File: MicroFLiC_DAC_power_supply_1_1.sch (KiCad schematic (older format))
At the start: 61 parts, among them P1 Socket_1x2, P2 Header_1x2, P3 Socket_2x4, U1 AP1117D50, U2 AP1117, U3 AP1117, U4 LM317, U5 LM317

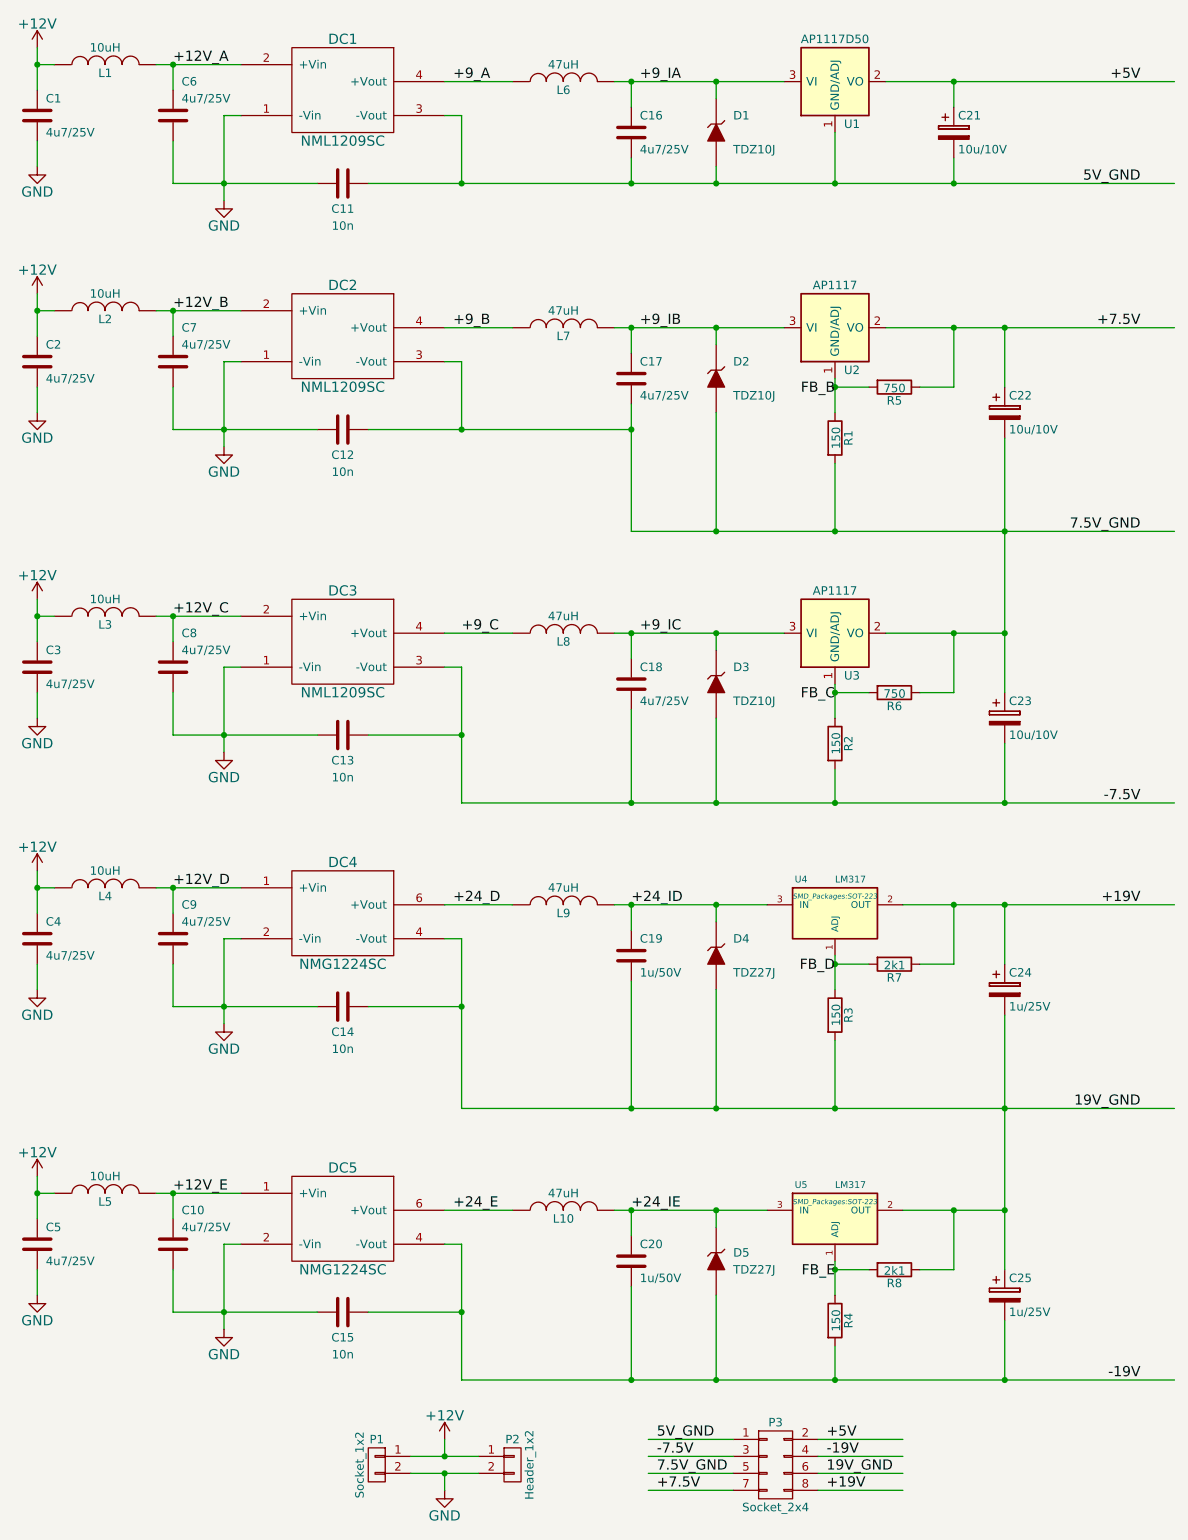
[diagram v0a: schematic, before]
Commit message: Completed part descriptions
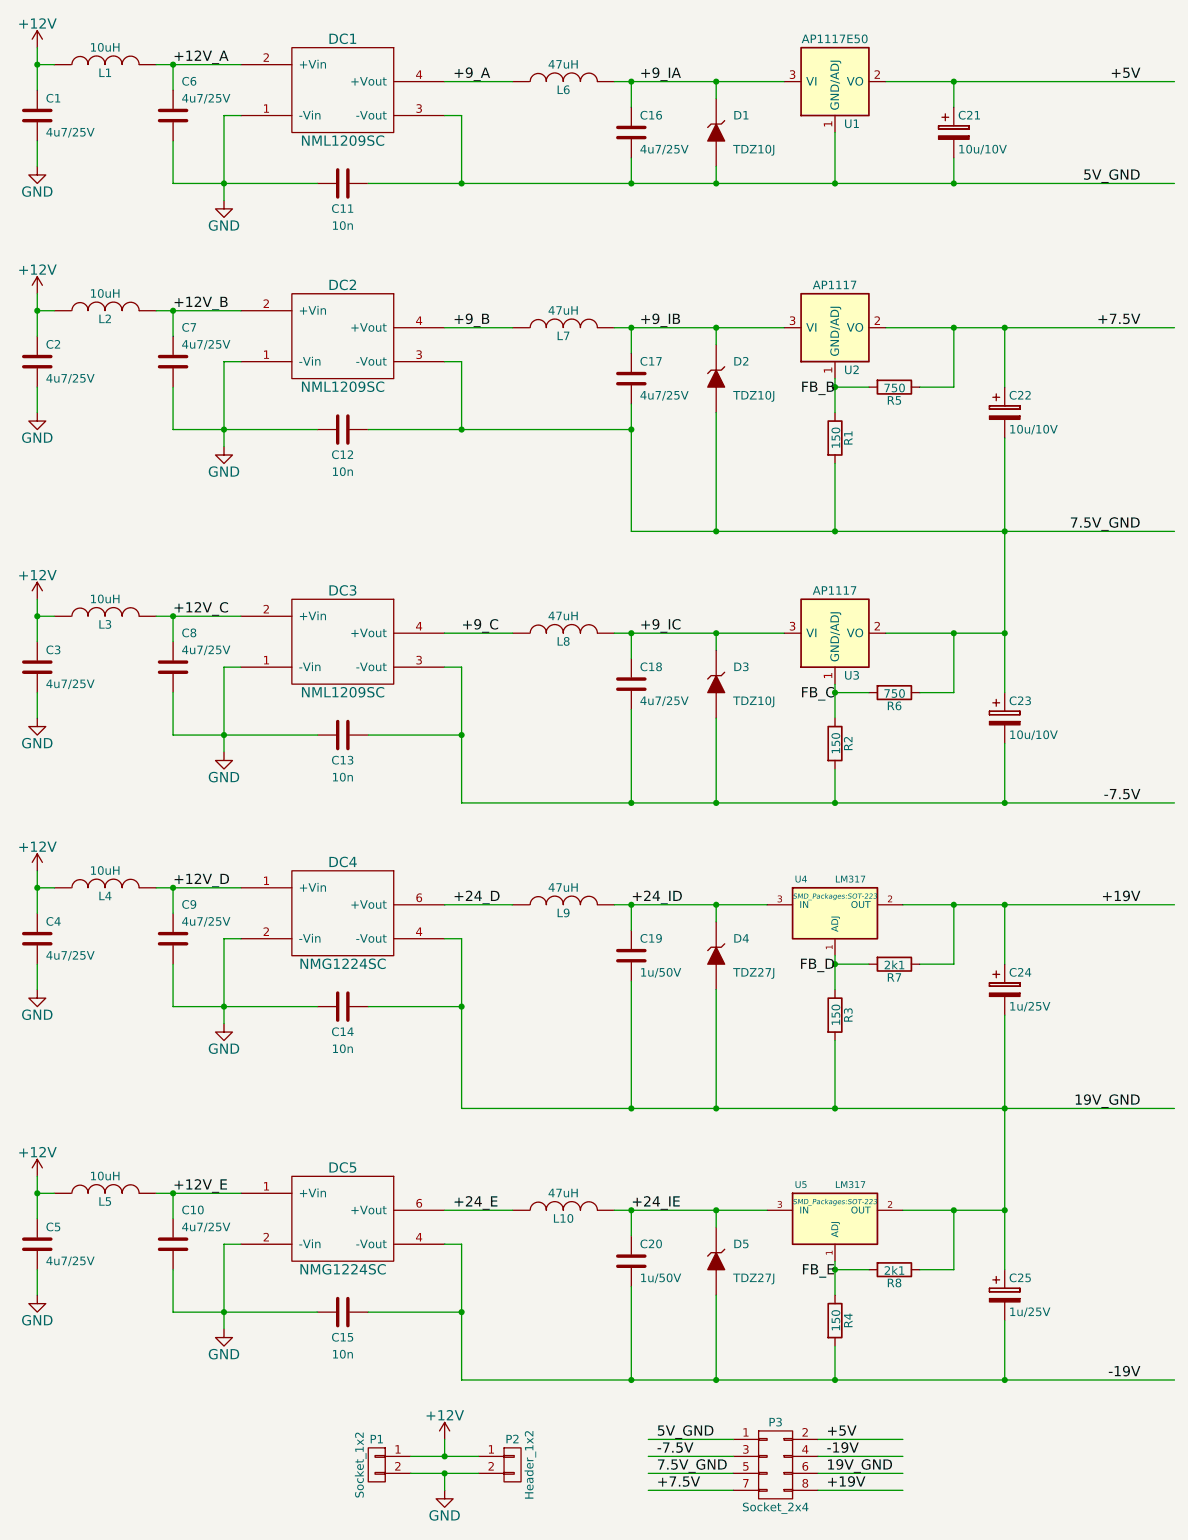
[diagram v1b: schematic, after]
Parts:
- C1, C10, C16, C17, C18, C2, C3, C4, C5, C6, C7, C8, C9: Alt. Order Code (none) -> 81-GRM21BR61E475MA2L; Alt. Supplier (none) -> Mouser; Note (none) -> 4μ7/25V X5R 0805 ceramic capacitor; Package (none) -> 0805; Supplier (none) -> Farnell
- C11, C12, C13, C14, C15: Note (none) -> Optional 10 nF X7R ceramic capacitor; Package (none) -> 0805; Supplier (none) -> Farnell
- C19, C20: Alt. Order Code (none) -> 81-GRM219R61H105KA3D; Alt. Supplier (none) -> Mouser; Note (none) -> 1μ/50V X5R 0805 ceramic capacitor; Package (none) -> 0805; Supplier (none) -> Farnell
- C21, C22, C23: Alt. Order Code (none) -> 581-TAJA106K010; Alt. Supplier (none) -> Mouser; Note (none) -> 10μF/10V/3Ω ESR tantalum capacitor; Package (none) -> case A; Supplier (none) -> Farnell
- C24, C25: Note (none) -> 1μ/25V/6.6Ω ESR tantalum capacitor; Package (none) -> case A; Supplier (none) -> Farnell
- D1, D2, D3: Alt. Order Code (none) -> 771-TDZ10J115; Alt. Supplier (none) -> Mouser; Note (none) -> 10V Zener diode; Package (none) -> SOD-323; Supplier (none) -> Farnell
- D4: Alt. Order Code (none) -> 771-TDZ27J115; Alt. Supplier (none) -> Mouser; Note (none) -> 27V Zener diode; Package (none) -> SOD-323; Supplier (none) -> Farnell
- D5: Alt. Order Code (none) -> 771-TDZ27J115; Alt. Supplier (none) -> Mouser; Note (none) -> 27V Zener diode; Package (none) -> SOD-323; Part Number (none) -> TDZ27J; Pert Number TDZ27J -> (none); Supplier (none) -> Farnell
- DC1, DC2, DC3: Alt. Order Code (none) -> 580-NML1209SC; Alt. Supplier (none) -> Mouser; Note (none) -> 12V in 9V out 2W DC-DC converter; Package (none) -> SIP-4; Supplier (none) -> Farnell
- DC4, DC5: Alt. Order Code (none) -> 81-NMG1224SC; Alt. Supplier (none) -> Mouser; Note (none) -> 12V in 24V out 2W DC-DC converter; Package (none) -> SIP-7; Supplier (none) -> Farnell
- L1, L2, L3, L4, L5: Alt. Order Code (none) -> 710-7440329100; Alt. Supplier (none) -> Mouser; Note (none) -> 10μH/0.45A SMD coil; Package (none) -> 1210; Supplier (none) -> Farnell
- L10, L6, L7, L8, L9: Alt. Order Code (none) -> 580-82473C; Alt. Supplier (none) -> Mouser; Note (none) -> 47μH/0.25A SMD coil; Package (none) -> 1210; Supplier (none) -> Farnell
- P1: Note (none) -> 1x2 ESQ series elevated socket strip; Package (none) -> SIL-2; Supplier (none) -> Farnell
- P2: Alt. Order Code (none) -> 855-M20-9990245; Alt. Supplier (none) -> Mouser; Note (none) -> 1x2 header strip; Package (none) -> SIL-2; Supplier (none) -> Farnell
- P3: Note (none) -> 2x4 ESQ series elevated socket strip; Package (none) -> DIL-8; Supplier (none) -> Farnell
- R1, R2, R3, R4: Note (none) -> 150Ω/1% 0805 resistor; Package (none) -> 0805; Supplier (none) -> Farnell
- R5: Note (none) -> 750Ω/1% 0805 resistor; Package (none) -> 0805; Supplier (none) -> Farnell
- R6: Note (none) -> 750Ω/1% 0805 resistor; Supplier (none) -> Farnell
- R7, R8: Alt. Order Code (none) -> 71-CRCW0805-2.1K-E3; Alt. Supplier (none) -> Mouser; Note (none) -> 2.1kΩ/1% 0805 resistor; Package (none) -> 0805; Supplier (none) -> Farnell
- U1: value AP1117D50 -> AP1117E50; Alt. Order Code (none) -> 621-AP1117E50G-13; Alt. Supplier (none) -> Mouser; Note (none) -> 5V linear voltage regulator; Package (none) -> SOT-223; Supplier (none) -> Farnell
- U2, U3: Alt. Order Code (none) -> 621-AP1117EG-13; Alt. Supplier (none) -> Mouser; Note (none) -> Adjustable linear voltage regulator; Package (none) -> SOT-223; Supplier (none) -> Farnell
- U4, U5: Alt. Order Code (none) -> 595-LM317DCY; Alt. Supplier (none) -> Mouser; Note (none) -> Adjustable linear voltage regulator; Package (none) -> SOT-223; Supplier (none) -> Farnell

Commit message: Added feedback filtering capacitors and protection diodes
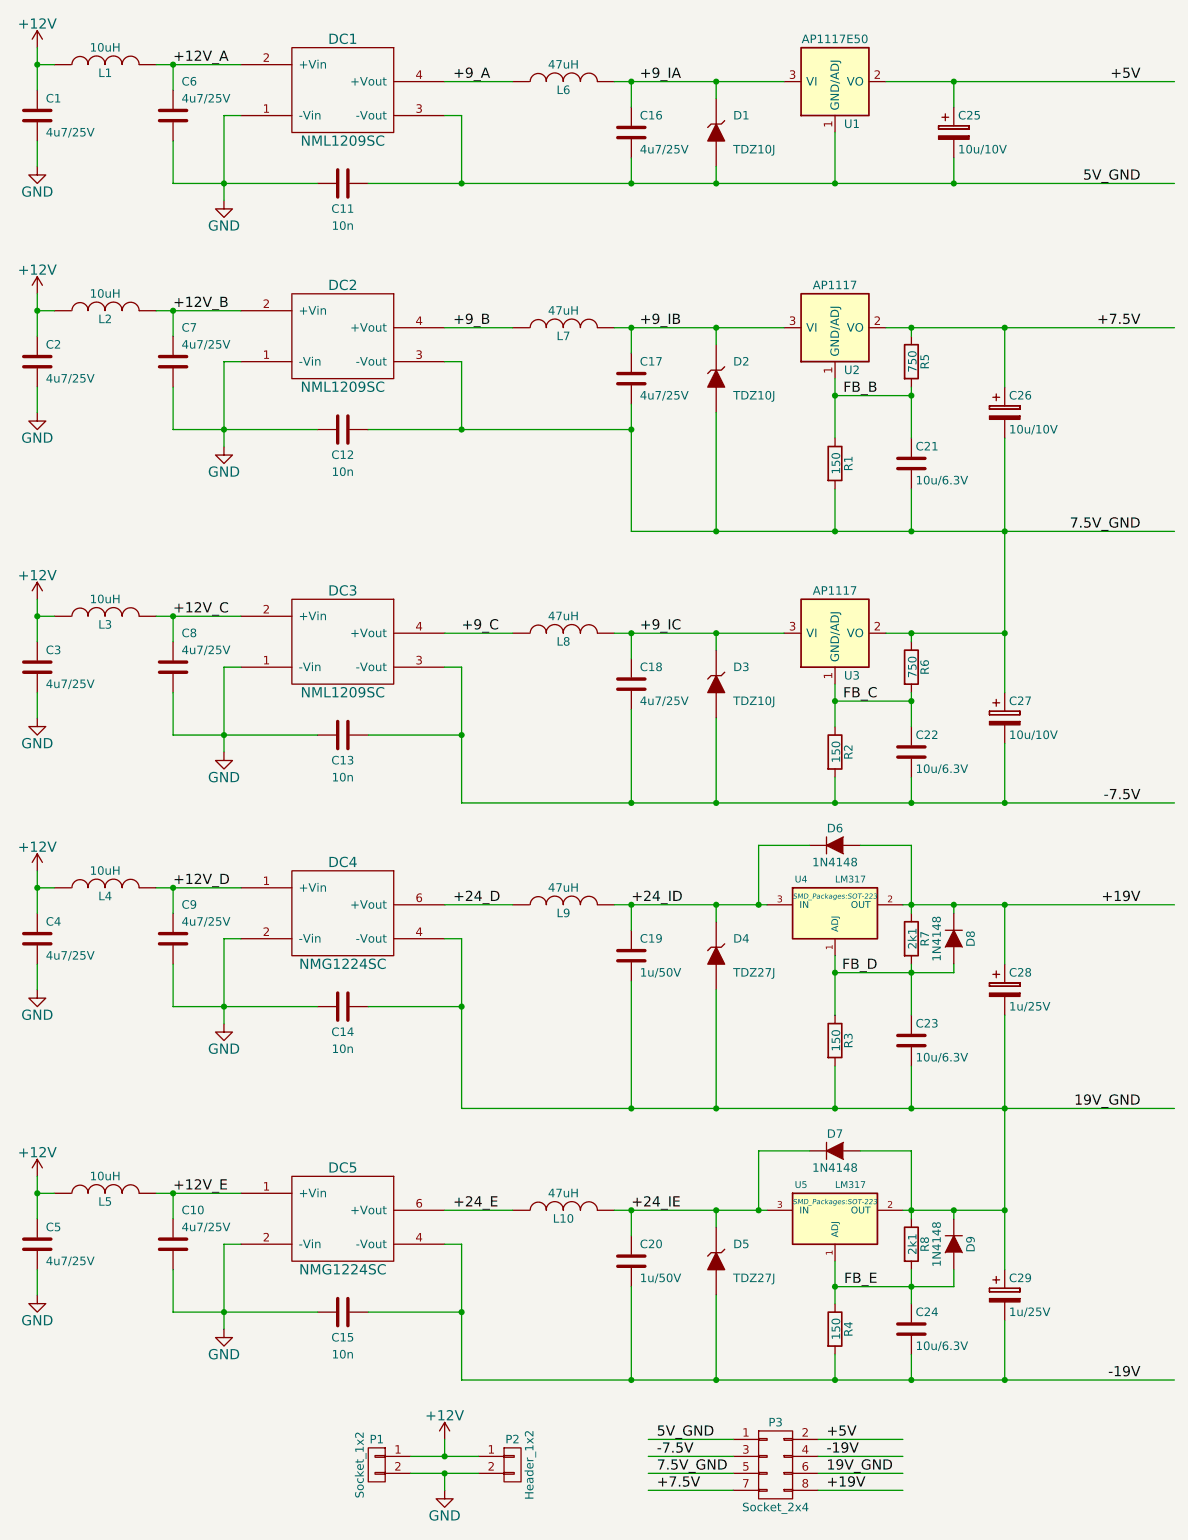
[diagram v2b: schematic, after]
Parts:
- added C21, C22, C23, C24: 10u/6.3V, Capacitors_SMD:C_0805, symbol C
- added D6, D7, D8, D9: 1N4148, Diodes_SMD:SOD-323, symbol D
- C11, C12, C13, C14, C15: Alt. Order Code (none) -> 80-C0805C103K5R; Alt. Supplier (none) -> Mouser
- C28: renamed from C24; Alt. Order Code (none) -> 74-TMCMA1E105MTRF; Alt. Supplier (none) -> Mouser
- C29: renamed from C25; Alt. Order Code (none) -> 74-TMCMA1E105MTRF; Alt. Supplier (none) -> Mouser
- P1: Alt. Order Code (none) -> ESQ-102-33-G-S; Alt. Supplier (none) -> Samtec
- P3: Alt. Order Code (none) -> ESQ-104-33-G-D; Alt. Supplier (none) -> Samtec
- R1, R2, R3, R4: Alt. Order Code (none) -> 71-TNPW0805150RFEEA; Alt. Supplier (none) -> Mouser
- R5, R6: Alt. Order Code (none) -> 603-RT0805FRE07750RL; Alt. Supplier (none) -> Mouser
- renumbered C21 to C25, C22 to C26, C23 to C27
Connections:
- wire segments 140 -> 154
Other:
- moved on the sheet: R1, R2, R3, R4, R5, R6, R7, R8

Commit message: Fixed capacitor order code
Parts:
- C11, C12, C13, C14, C15: Order Code 9306352 -> 9406352
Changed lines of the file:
@@
 F 6 "0805" H 2500 1600 60  0001 C CNN "Package"
 F 7 "Farnell" H 2500 1600 60  0001 C CNN "Supplier"
-F 8 "9306352" V 2500 1600 60  0001 C CNN "Order Code"
+F 8 "9406352" V 2500 1600 60  0001 C CNN "Order Code"
 F 9 "Mouser" H 2500 1600 60  0001 C CNN "Alt. Supplier"
 F 10 "80-C0805C103K5R" H 2500 1600 60  0001 C CNN "Alt. Order Code"
@@
 F 6 "0805" H 2500 3050 60  0001 C CNN "Package"
 F 7 "Farnell" H 2500 3050 60  0001 C CNN "Supplier"
-F 8 "9306352" V 2500 3050 60  0001 C CNN "Order Code"
+F 8 "9406352" V 2500 3050 60  0001 C CNN "Order Code"
 F 9 "Mouser" H 2500 3050 60  0001 C CNN "Alt. Supplier"
 F 10 "80-C0805C103K5R" H 2500 3050 60  0001 C CNN "Alt. Order Code"
@@
 F 6 "0805" H 2500 4850 60  0001 C CNN "Package"
 F 7 "Farnell" H 2500 4850 60  0001 C CNN "Supplier"
-F 8 "9306352" V 2500 4850 60  0001 C CNN "Order Code"
+F 8 "9406352" V 2500 4850 60  0001 C CNN "Order Code"
 F 9 "Mouser" H 2500 4850 60  0001 C CNN "Alt. Supplier"
 F 10 "80-C0805C103K5R" H 2500 4850 60  0001 C CNN "Alt. Order Code"
@@
 F 6 "0805" H 2500 6450 60  0001 C CNN "Package"
 F 7 "Farnell" H 2500 6450 60  0001 C CNN "Supplier"
-F 8 "9306352" V 2500 6450 60  0001 C CNN "Order Code"
+F 8 "9406352" V 2500 6450 60  0001 C CNN "Order Code"
 F 9 "Mouser" H 2500 6450 60  0001 C CNN "Alt. Supplier"
 F 10 "80-C0805C103K5R" H 2500 6450 60  0001 C CNN "Alt. Order Code"
@@
 F 6 "0805" H 2500 8250 60  0001 C CNN "Package"
 F 7 "Farnell" H 2500 8250 60  0001 C CNN "Supplier"
-F 8 "9306352" V 2500 8250 60  0001 C CNN "Order Code"
+F 8 "9406352" V 2500 8250 60  0001 C CNN "Order Code"
 F 9 "Mouser" H 2500 8250 60  0001 C CNN "Alt. Supplier"
 F 10 "80-C0805C103K5R" H 2500 8250 60  0001 C CNN "Alt. Order Code"
